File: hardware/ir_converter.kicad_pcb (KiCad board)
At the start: 2 copper layers, 38.1 x 53.1 mm, 47 parts, among them J1 MX-47346-0001, J2 SWD, J3 TP, J4 TP, Q1 LL-S350PTC-1A, SW1 RESET, SW2 SW2, U1 TLV70033DDCT, U2 USBLC6-2, U3 STM32F103C8T6

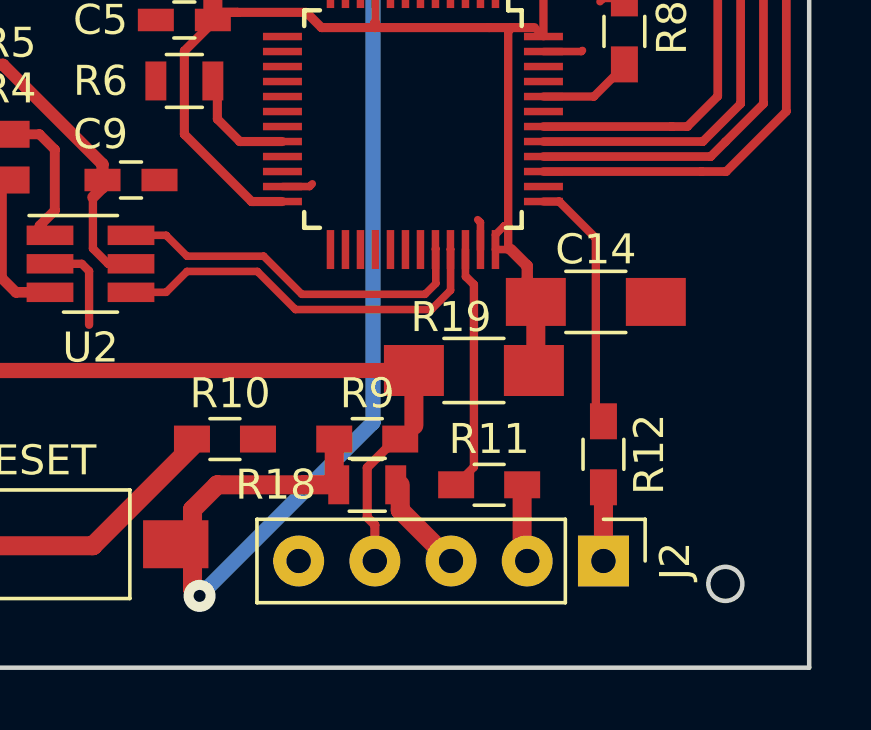
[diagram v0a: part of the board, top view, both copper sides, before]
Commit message: Changed ground plane clearance
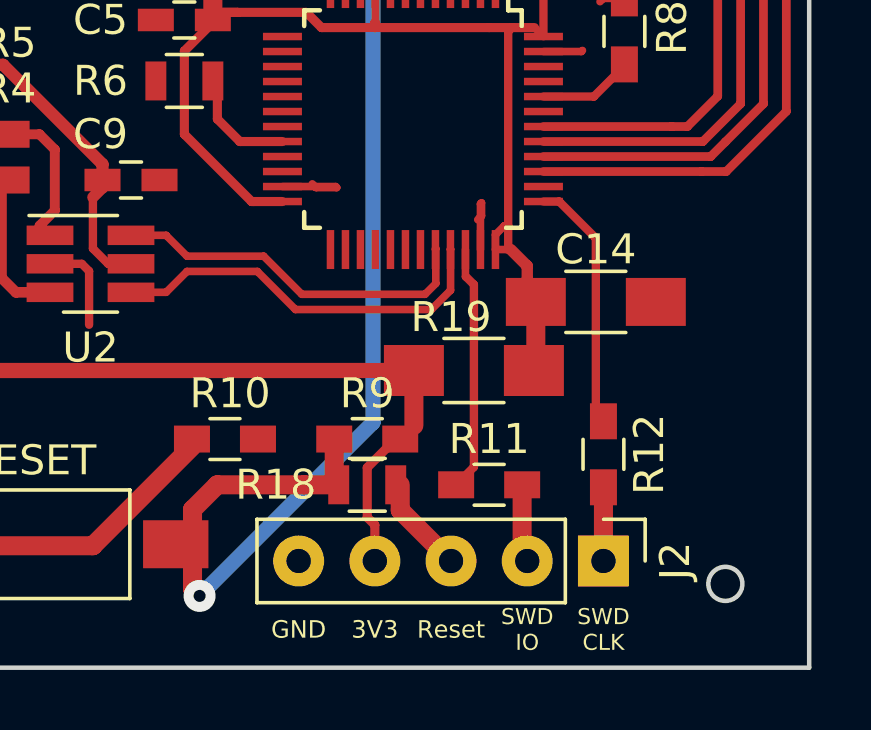
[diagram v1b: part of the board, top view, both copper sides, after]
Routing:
- net GND: track 17.2 -> 20.0 mm
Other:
- board text added: "3V3"
- board text added: "GND"
- board text added: "Reset"
- board text added: "SWD CLK"
- board text added: "SWD IO"
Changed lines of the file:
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@@
     (links 97)
     (no_connects 3)
-    (area 50.824001 62.738 157.757715 162.212001)
+    (area 77.394999 88.570999 115.645001 141.807001)
     (thickness 1.6)
-    (drawings 34)
-    (tracks 273)
+    (drawings 39)
+    (tracks 277)
     (zones 0)
     (modules 47)
@@
     (user_trace_width 0.635)
     (trace_clearance 0.2)
-    (zone_clearance 0.2794)
+    (zone_clearance 0.3302)
     (zone_45_only yes)
     (trace_min 0.2)
@@
       (outputformat 4)
       (mirror true)
-      (drillshape 2)
+      (drillshape 0)
       (scaleselection 1)
       (outputdirectory documentation/))
@@
     )
   )
+  (gr_text 3V3 (at 101.092 140.462) (layer F.SilkS)
+    (effects (font (size 0.5842 0.5842) (thickness 0.14605)))
+  )
+  (gr_text GND (at 98.552 140.462) (layer F.SilkS)
+    (effects (font (size 0.5842 0.5842) (thickness 0.14605)))
+  )
+  (gr_text Reset (at 103.632 140.462) (layer F.SilkS)
+    (effects (font (size 0.5842 0.5842) (thickness 0.14605)))
+  )
+  (gr_text "SWD\nCLK\n" (at 108.712 140.462) (layer F.SilkS)
+    (effects (font (size 0.5334 0.5334) (thickness 0.13335)))
+  )
+  (gr_text "SWD\nIO" (at 106.172 140.462) (layer F.SilkS)
+    (effects (font (size 0.5334 0.5334) (thickness 0.127)))
+  )
   (gr_circle (center 80.264 99.06) (end 80.518 99.568) (layer Edge.Cuts) (width 0.15))
   (dimension 2.794 (width 0.3) (layer Dwgs.User)
@@
   (segment (start 86.328 117.602) (end 86.36 117.634) (width 0.635) (layer F.Cu) (net 1))
   (segment (start 86.022 117.296) (end 86.36 117.634) (width 0.635) (layer F.Cu) (net 1))
+  (segment (start 104.612 127.794) (end 104.612 126.274) (width 0.254) (layer F.Cu) (net 2))
+  (segment (start 104.612 126.274) (end 104.648 126.238) (width 0.254) (layer F.Cu) (net 2))
+  (segment (start 104.648 126.238) (end 104.648 126.672) (width 0.254) (layer F.Cu) (net 2))
+  (segment (start 104.648 126.672) (end 104.521 126.799) (width 0.254) (layer F.Cu) (net 2))
+  (segment (start 98.012 125.694) (end 99.786 125.694) (width 0.254) (layer F.Cu) (net 2))
+  (segment (start 99.786 125.694) (end 99.822 125.73) (width 0.254) (layer F.Cu) (net 2))
+  (segment (start 99.822 125.73) (end 99.134 125.73) (width 0.254) (layer F.Cu) (net 2))
+  (segment (start 99.134 125.73) (end 99.007 125.603) (width 0.254) (layer F.Cu) (net 2))
   (segment (start 79.375 122.047) (end 80.899 122.047) (width 0.254) (layer F.Cu) (net 2))
   (segment (start 80.899 122.047) (end 81.534 122.682) (width 0.254) (layer F.Cu) (net 2))
@@
   (segment (start 90.264 128.27) (end 91.3234 128.27) (width 0.2794) (layer F.Cu) (net 2))
   (segment (start 91.3234 128.27) (end 91.567 128.5136) (width 0.2794) (layer F.Cu) (net 2))
-  (segment (start 98.012 125.694) (end 98.916 125.694) (width 0.254) (layer F.Cu) (net 2))
-  (segment (start 98.916 125.694) (end 99.007 125.603) (width 0.254) (layer F.Cu) (net 2))
-  (segment (start 104.612 127.794) (end 104.612 126.89) (width 0.254) (layer F.Cu) (net 2))
-  (segment (start 104.612 126.89) (end 104.521 126.799) (width 0.254) (layer F.Cu) (net 2))
   (segment (start 100.904 110.236) (end 100.904 112.592) (width 0.635) (layer F.Cu) (net 3))
   (segment (start 100.904 112.592) (end 99.704 113.792) (width 0.635) (layer F.Cu) (net 3))
@@
   (segment (start 92.014 125.73) (end 91.694 126.05) (width 0.381) (layer F.Cu) (net 59))
   (zone (net 2) (net_name GND) (layer F.Cu) (hatch edge 0.508)
-    (connect_pads (clearance 0.2794))
+    (connect_pads (clearance 0.3302))
     (min_thickness 0.254)
     (fill yes (arc_segments 16) (thermal_gap 0.508) (thermal_bridge_width 0.508) (smoothing chamfer))

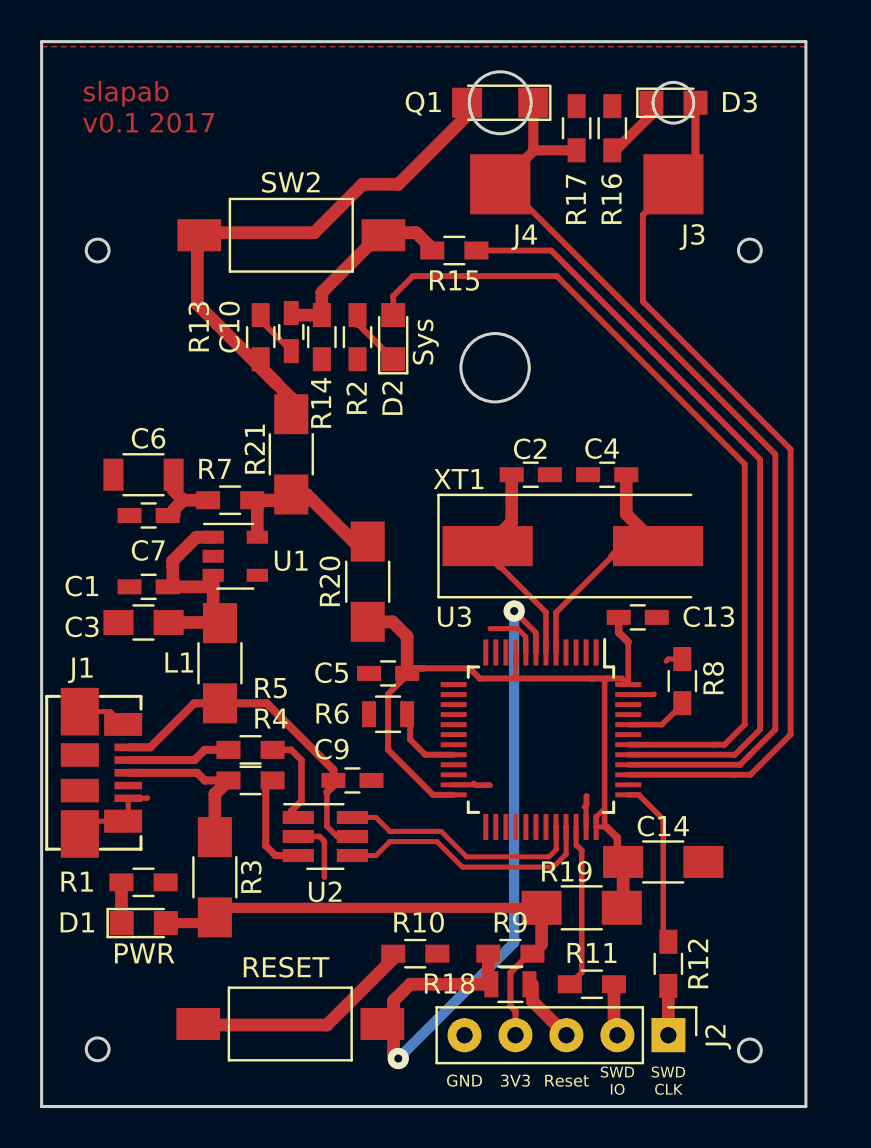
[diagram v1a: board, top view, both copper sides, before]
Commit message: Added npn tranistor to drive the IR LED.
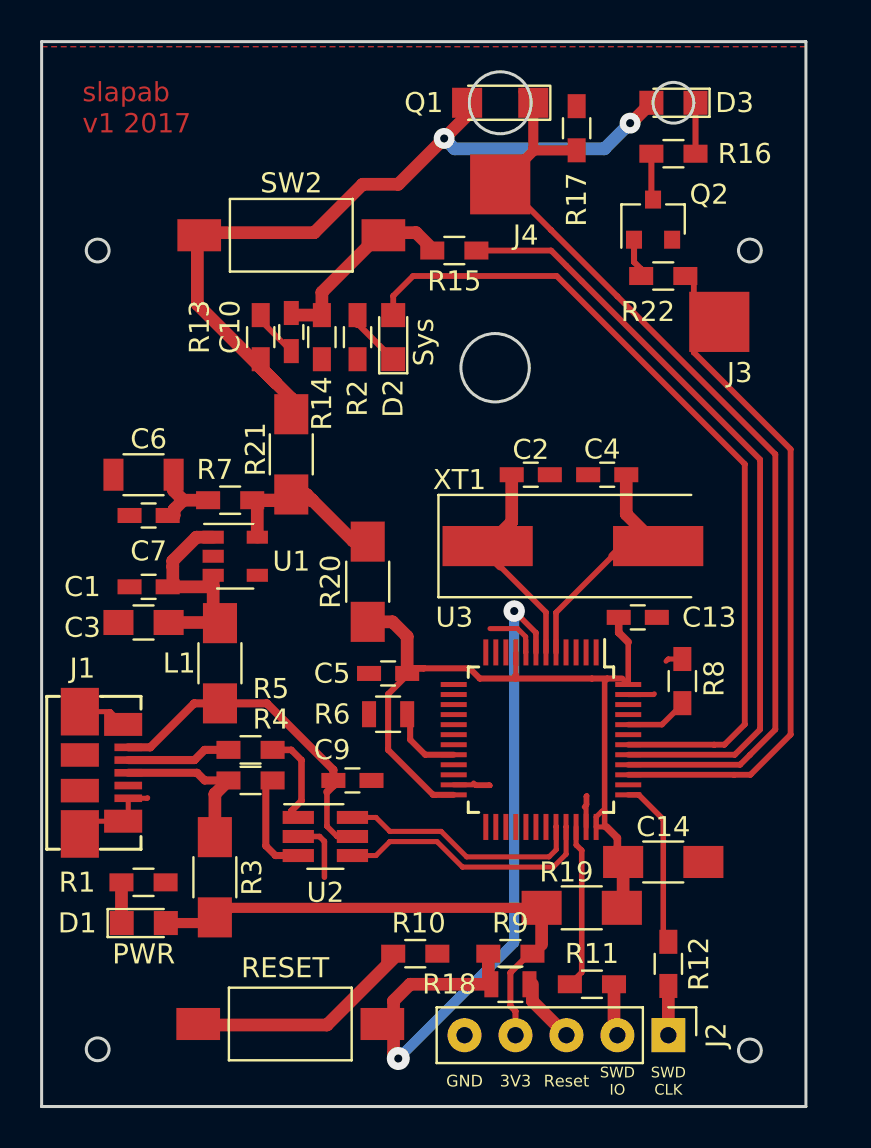
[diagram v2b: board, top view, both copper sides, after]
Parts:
- added Q2: BC817-40, TO_SOT_Packages_SMD:SOT-23, F.Cu at (108.0, 97.5)
- added R22: 1k, Resistors_SMD:R_0603_HandSoldering, F.Cu at (108.5, 100.3)
- R10, R15: value 330R -> 560R
- R16: value 460R -> 49R
- R17: value 2k -> 1k
- moved J3 7.23 mm to (111.3, 102.6)
- moved R16 3.30 mm to (109.0, 94.2), turned to 0 degrees
- turned D3 to 180 degrees
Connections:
- D3 pad 2: /IR_CLK -> +3V3
- R16 pad 1: GND -> Net-(Q2-Pad3)
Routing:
- net +3V3: track 110.8 -> 122.3 mm, vias 0 -> 2
- net /IR_CLK: track 44.6 -> 35.8 mm
- net Net-(Q2-Pad3): track 0.00 -> 2.32 mm
- net Net-(Q2-Pad1): track 0.00 -> 1.96 mm
- net Net-(D3-Pad1): track 3.33 -> 2.54 mm
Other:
- net class 3v3: via_dia 0.6 -> 1.0414
- net class Default: via_dia 0.6 -> 0.889
- board text added: "slapab v1 2017"
- board text removed: "slapab v0.1 2017"

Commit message: Added bug fixes on schematic. Redesigning PCB.
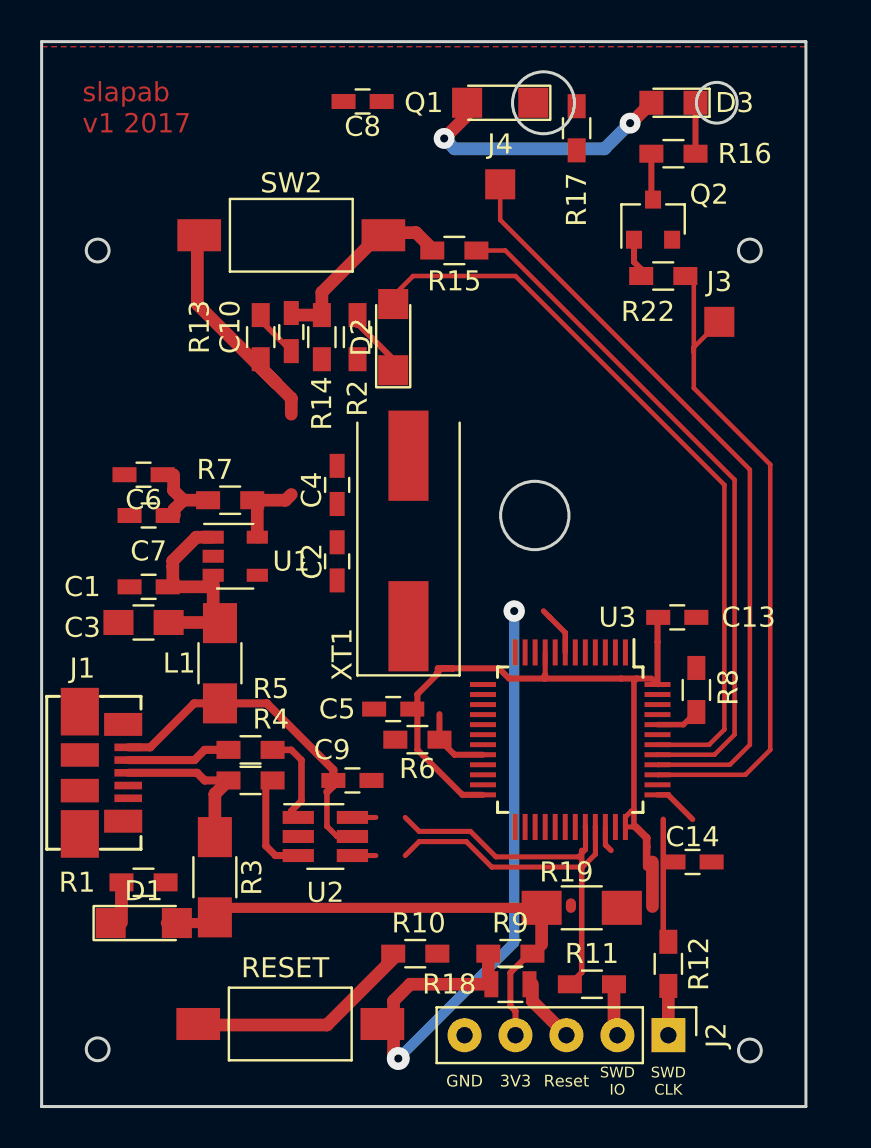
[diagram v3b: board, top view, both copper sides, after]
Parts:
- removed R20, R21: 0R, Resistors_SMD:R_1206_HandSoldering
- added C8: 1uF, Capacitors_SMD:C_0603_HandSoldering, F.Cu at (93.5, 91.6)
- C14: footprint Capacitors_SMD:C_1206_HandSoldering -> Capacitors_SMD:C_0603_HandSoldering
- C6: footprint Capacitors_SMD:C_1206 -> Capacitors_SMD:C_0603_HandSoldering
- D1, D2: footprint LEDs:LED_0805 -> LEDs:LED_1206
- J3, J4: footprint Measurement_Points:Measurement_Point_Square-SMD-Pad_Big -> Measurement_Points:Measurement_Point_Square-SMD-Pad_Small
- R1, R2: value 460R -> 1.2k
- R17, R22: value 1k -> 1.2k
- R6: footprint Resistors_SMD:R_0805 -> Resistors_SMD:R_0603_HandSoldering
- R7: value 1R -> 0.01R
- moved C4 13.5 mm to (92.2, 110.7), turned to 270 degrees
- moved C2 10.6 mm to (92.2, 114.6), turned to 90 degrees
- moved XT1 8.20 mm to (95.8, 113.5), turned to 90 degrees
- moved C13 1.97 mm to (109.2, 117.3)
- moved R6 1.94 mm to (96.2, 123.4)
- moved C5 1.80 mm to (95.0, 121.9)
- moved U3 1.46 mm to (103.8, 123.4)
- moved C14 1.46 mm to (109.9, 129.5)
- moved R8 0.83 mm to (110.1, 121.0)
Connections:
- Q1 pad 1: /IR_IN -> GND
- Q1 pad 2: +3V3 -> /IR_IN
- R17 pad 1: GND -> /IR_IN
- R17 pad 2: /IR_IN -> +3V3
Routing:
- net +3V3: track 122.3 -> 91.2 mm
- net GND: track 20.0 -> 0.78 mm
- net /IR_IN: track 53.5 -> 40.3 mm
- net /OSC_IN: track 12.7 -> 0.00 mm
- net /OSC_OUT: track 11.4 -> 0.00 mm
- net /SW_USER: track 39.1 -> 34.7 mm
- net /LED1: track 42.0 -> 38.0 mm
- net (no net): track 0.00 -> 2.53 mm
- net /IR_CLK: track 35.8 -> 33.4 mm
- net /BOOT0: track 3.10 -> 2.20 mm
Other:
- outline, holes or cut-outs redrawn
- net class 3v3: clearance 0.2 -> 0.2032; via_dia 1.0414 -> 0.889; via_drill 0.4 -> 0.3
- net class Default: clearance 0.2 -> 0.2032; trace_width 0.3302 -> 0.254; via_drill 0.4 -> 0.3
- rule trace_clearance: 0.2 -> 0.2032
- rule trace_min: 0.2 -> 0.2032
- rule via_min_drill: 0.300228 -> 0.3
- rule via_min_size: 0.4 -> 0.5

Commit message: Elements arrangement.
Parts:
- removed R19: 0R, Resistors_SMD:R_1206_HandSoldering
- removed R7: 0.01R, Resistors_SMD:R_0603_HandSoldering
- R18: footprint Resistors_SMD:R_0805 -> Resistors_SMD:R_0603_HandSoldering
- R3: footprint Resistors_SMD:R_1206_HandSoldering -> Resistors_SMD:R_0603_HandSoldering
- moved D1 19.3 mm to (87.1, 113.8), turned to 270 degrees
- moved R1 18.8 mm to (89.4, 113.0), turned to 270 degrees
- moved C8 14.0 mm to (107.4, 91.7)
- moved R10 12.7 mm to (83.6, 135.9), turned to 90 degrees
- moved C6 8.48 mm to (83.8, 118.6), turned to 270 degrees
- moved C1 7.91 mm to (88.1, 121.7)
- moved C3 7.91 mm to (87.9, 123.4)
- moved L1 7.03 mm to (91.7, 124.2)
- moved C7 6.84 mm to (85.3, 118.6), turned to 270 degrees
- moved R4 6.06 mm to (91.2, 130.6)
- moved R5 5.85 mm to (91.2, 128.8)
- moved J1 5.48 mm to (83.6, 129.0)
- moved R3 5.47 mm to (91.2, 132.3), turned to 0 degrees
- moved R2 5.09 mm to (98.3, 103.6), turned to 180 degrees
- moved R8 4.90 mm to (109.7, 116.1)
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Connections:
- net Net-(J1-Pad2) renamed /S_D-
- net Net-(J1-Pad3) renamed /S_D+
- C6 pad 1: Net-(C6-Pad1) -> +3V3
- C7 pad 1: Net-(C6-Pad1) -> +3V3
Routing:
- net +3V3: track 91.2 -> 35.4 mm, vias 2 -> 0
- net /RESET: track 36.4 -> 10.9 mm, vias 2 -> 0
- net Net-(R10-Pad1): track 10.8 -> 0.00 mm
- net +5V: track 10.9 -> 1.80 mm
- net /IR_CLK: track 33.4 -> 24.3 mm
- net /LED1: track 38.0 -> 29.2 mm
- net /BOOT0: track 2.20 -> 6.67 mm
- net /SWDIO: track 8.21 -> 4.20 mm
- net /IR_IN: track 40.3 -> 44.3 mm
- net Net-(C6-Pad1): track 3.98 -> 0.00 mm
- net /BOOT1: track 3.75 -> 0.00 mm
- net /USB_D+: track 13.1 -> 9.77 mm
- net Net-(R5-Pad1): track 5.30 -> 2.07 mm
- net Net-(R4-Pad1): track 5.27 -> 2.12 mm
- net /USB_D-: track 12.3 -> 9.77 mm
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
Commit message: Almost done.
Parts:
- D3: footprint LEDs:LED_0805 -> CustomFootprints:IR_LED_WIDE
- Q1: footprint LEDs:LED_1206 -> CustomFootprints:IR_PHOTO_WIDE
- moved J4 4.79 mm to (100.1, 94.5)
- moved C8 2.90 mm to (105.7, 94.0)
- moved R17 1.61 mm to (105.7, 95.5)
- moved C1 1.52 mm to (86.6, 121.7)
- moved C3 1.52 mm to (86.4, 123.4)
- moved C13 1.48 mm to (108.0, 117.5)
- moved R8 1.46 mm to (109.7, 117.5)
- moved L1 1.27 mm to (90.4, 124.2)
- moved C2 1.14 mm to (92.2, 115.7)
- moved C4 1.14 mm to (92.2, 111.9)
- moved Q2 1.14 mm to (110.2, 97.8)
- moved R22 1.14 mm to (107.7, 99.8)
- moved J3 1.05 mm to (109.5, 101.1)
- moved C5 0.51 mm to (96.3, 124.5)
- moved R6 0.51 mm to (96.2, 122.9)
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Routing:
- net +3V3: track 35.4 -> 147.2 mm, vias 0 -> 25
- net /RESET: track 10.9 -> 34.4 mm, vias 0 -> 2
- net /OSC_IN: track 0.00 -> 21.3 mm
- net /OSC_OUT: track 0.00 -> 14.0 mm
- net GND: track 0.00 -> 6.83 mm
- net /IR_CLK: track 24.3 -> 30.7 mm
- net Net-(D3-Pad1): track 0.00 -> 3.48 mm
- net /BOOT1: track 0.00 -> 3.16 mm
- net Net-(R10-Pad1): track 0.00 -> 2.71 mm
- net Net-(Q2-Pad3): track 0.00 -> 1.85 mm
- net Net-(Q2-Pad1): track 0.00 -> 1.61 mm
- net /BOOT0: track 6.67 -> 5.60 mm
- net +5V: track 1.80 -> 0.83 mm
- net /IR_IN: track 44.3 -> 43.7 mm
- added copper zone on B.Cu, net +3V3
- added copper zone on F.Cu, net +3V3
- added copper zone on F.Cu, net +5V
- added copper zone on B.Cu, net GND
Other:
- board size 38.1 x 53.1 mm -> 37.3 x 52.1 mm
- net class 3v3: via_dia 0.889 -> 0.762
- net class Default: via_dia 0.889 -> 0.762
- rule via_min_size: 0.5 -> 0.635
- board text added: "R"
- board text added: "SCLK"
- board text added: "SIO"
- board text added: "slapab v2 2017"
- board text removed: "Reset"
- board text removed: "SWD CLK"
- board text removed: "SWD IO"
- board text removed: "slapab v1 2017"
